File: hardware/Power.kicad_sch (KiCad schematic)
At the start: 19 parts, among them J10 DC, Q1 Q_NMOS, U10 ADP7142AUJZ-3.3, U11 ADP7142AUJZ-2.5, U12 LM74700, U13 ADP7142AUJZ-5.0

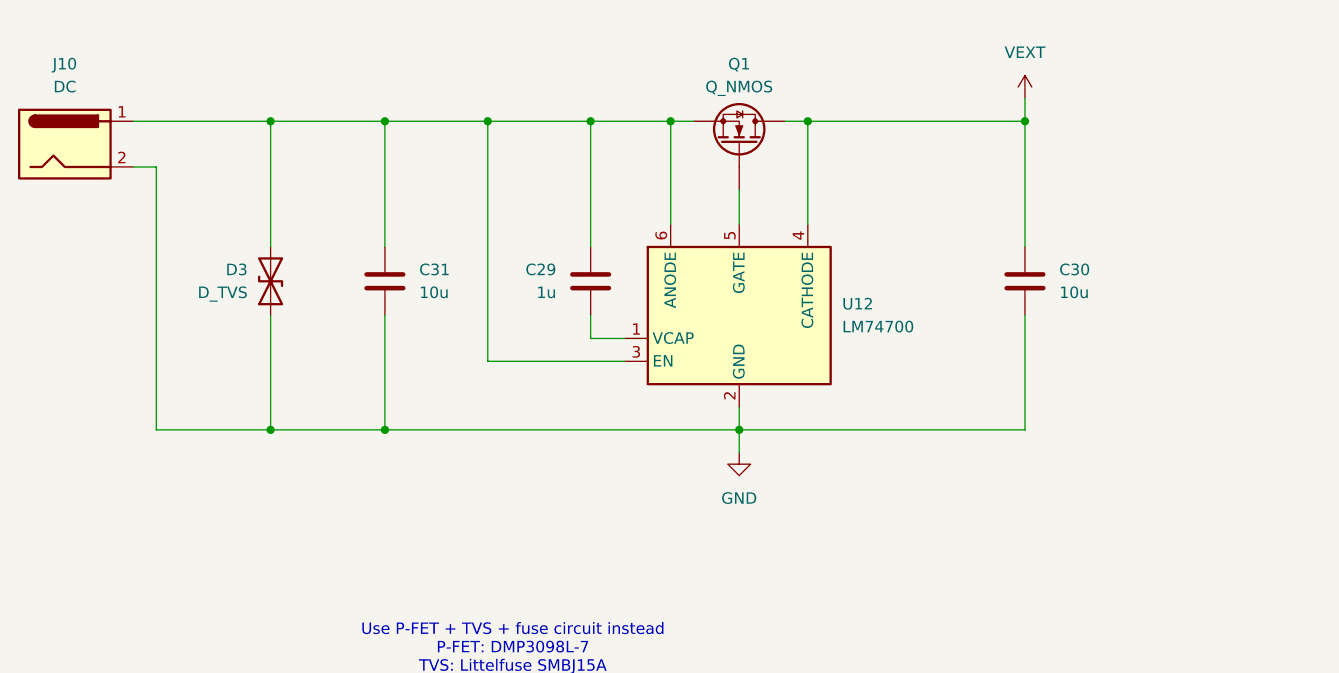
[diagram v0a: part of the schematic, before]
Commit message: updated Power input on schematic
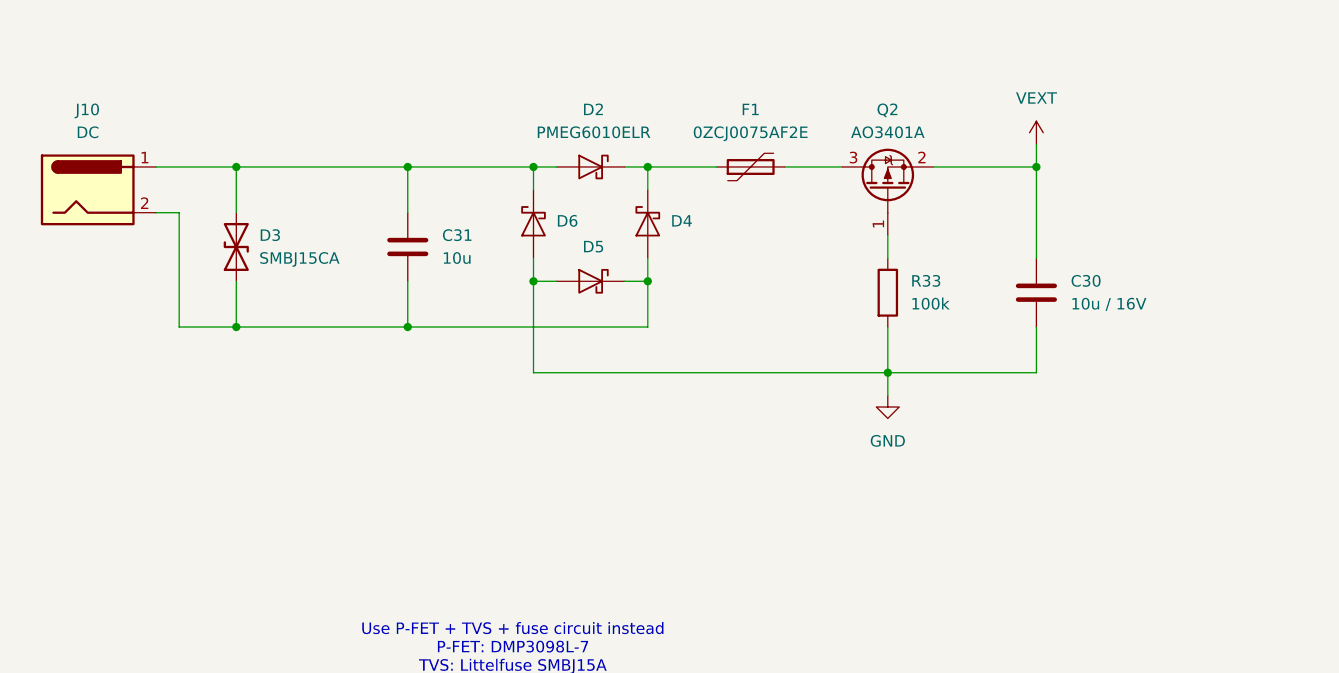
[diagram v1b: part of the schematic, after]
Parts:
- removed C29: 1u, Capacitor_SMD:C_0603_1608Metric, symbol Device:C
- removed Q1: Q_NMOS, symbol Device:Q_NMOS
- removed U12: LM74700, Package_TO_SOT_SMD:SOT-23-6, symbol Power_Management:LM74700
- added D2, D4, D5, D6: PMEG6010ELR, Diode_SMD:Nexperia_CFP3_SOD-123W, symbol Diode:PMEG6010ELR
- added F1: 0ZCJ0075AF2E, symbol Device:Polyfuse
- added Q2: AO3401A, Package_TO_SOT_SMD:SOT-23, symbol Transistor_FET:AO3401A
- added R33: 100k, symbol Device:R
- C30: value 10u -> 10u / 16V
- D3: value D_TVS -> SMBJ15CA
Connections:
- net GND: now also D5.2 (A), D6.2 (A), R33.2; no longer C31.2, D3.1 (A1), J10.2
- net VEXT: now also Q2.2 (S)
- net at C31.1, D3.2 (A2), J10.1: now also D2.2 (A), D6.1 (K)
- new net: D2.1 (K), D4.1 (K), F1.1
- new net: C31.2, D3.1 (A1), D4.2 (A), D5.1 (K), J10.2
- new net: Q2.1 (G), R33.1
- new net: F1.2, Q2.3 (D)
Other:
- moved on the sheet: C31, D3, J10

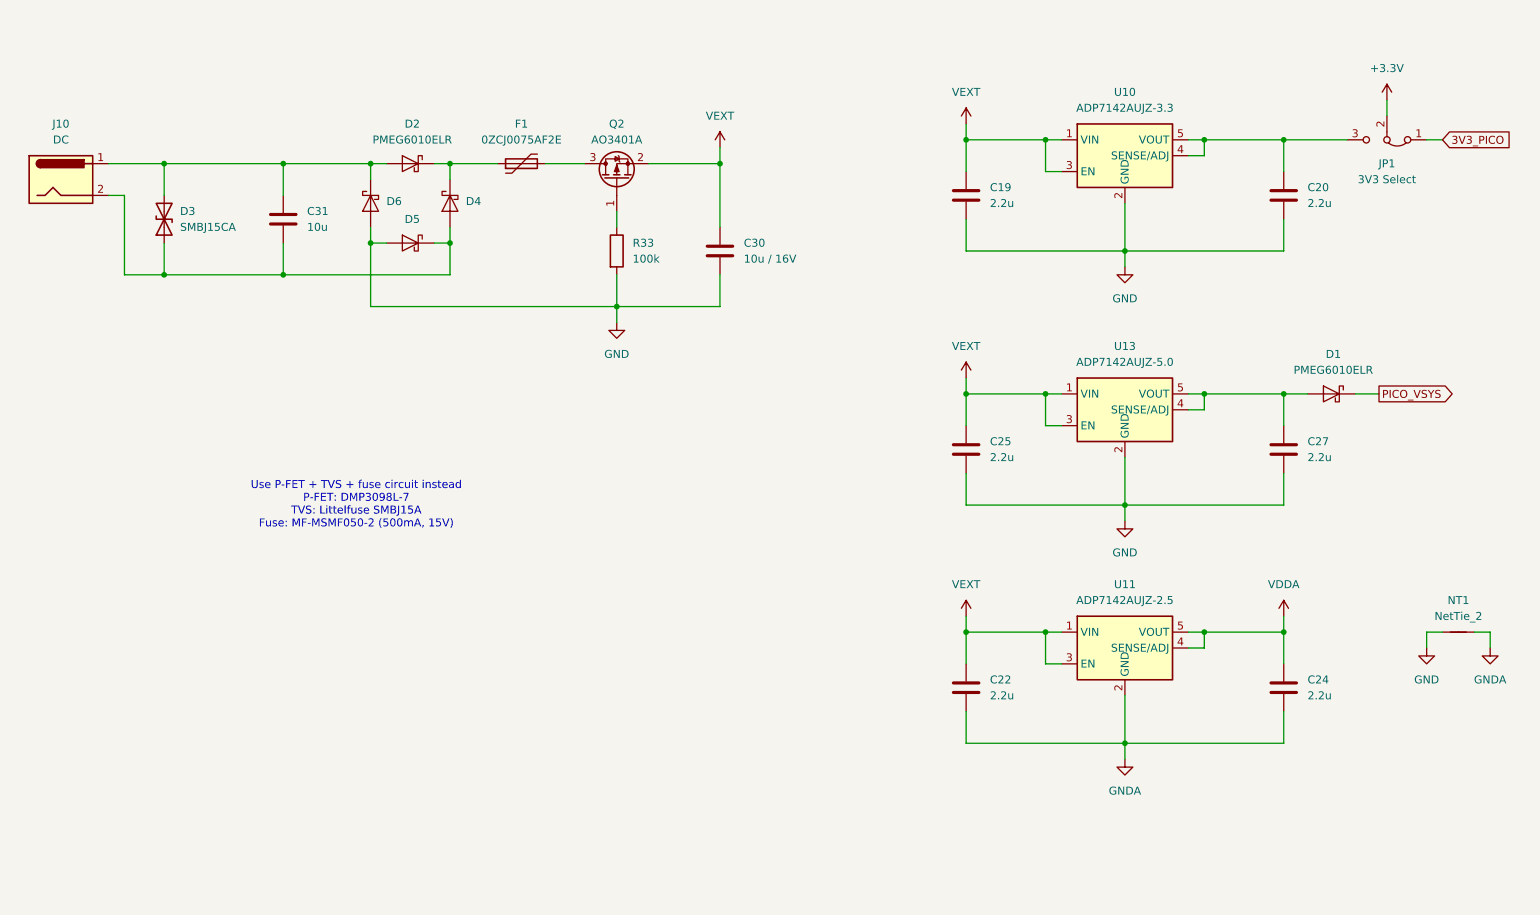
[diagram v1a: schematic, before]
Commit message: reworked power protection circuit and fixed ERC errors
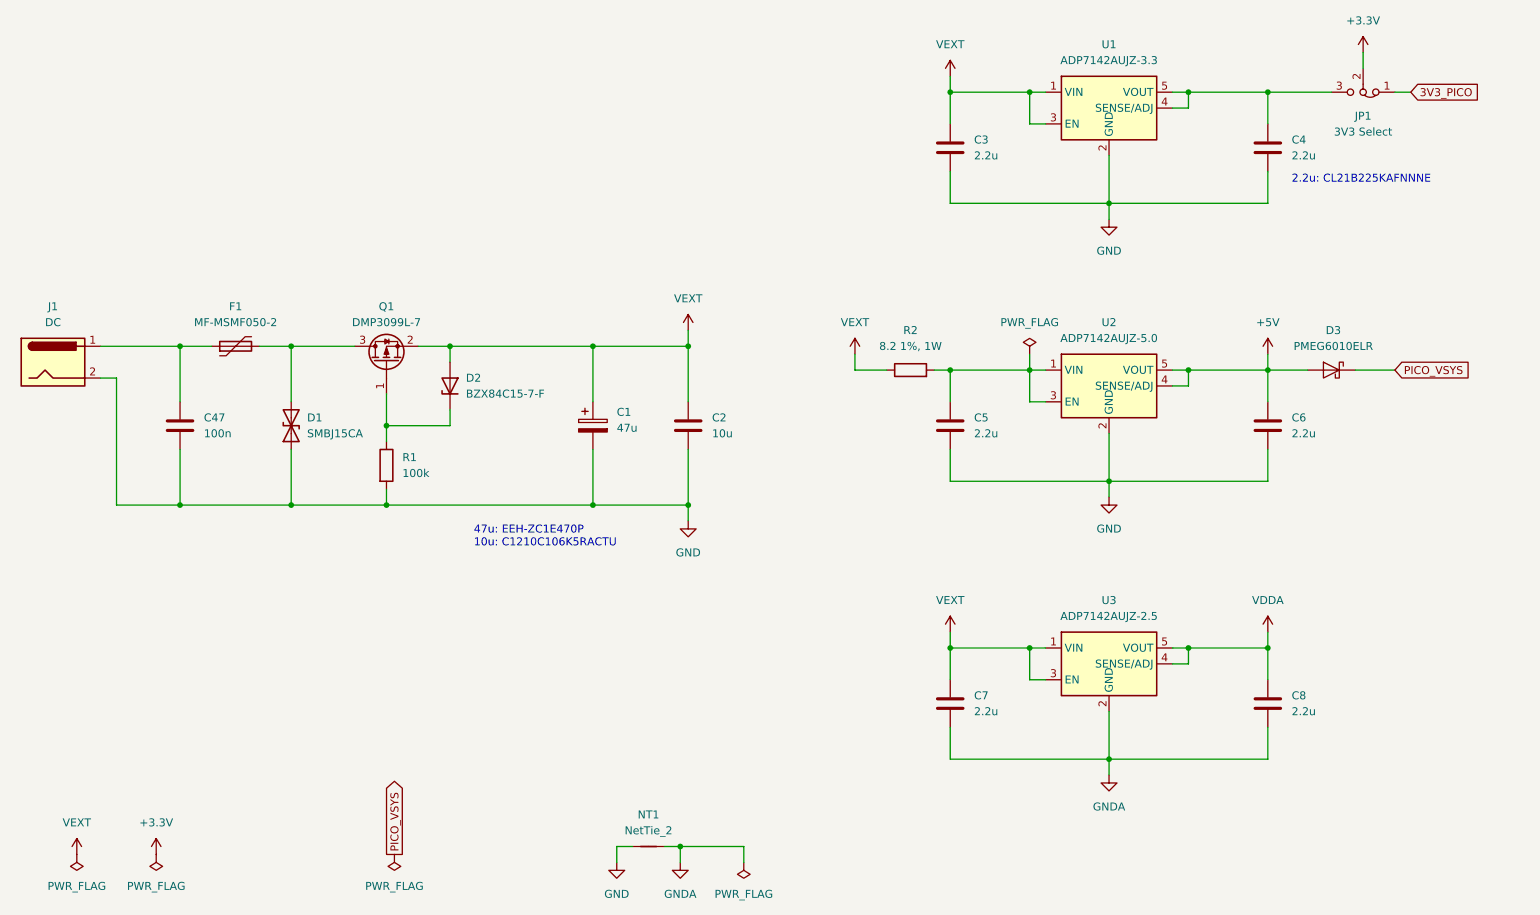
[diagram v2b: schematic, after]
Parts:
- removed C30: 10u / 16V, Capacitor_SMD:C_0603_1608Metric, symbol Device:C
- removed C31: 10u, Capacitor_SMD:C_0603_1608Metric, symbol Device:C
- removed D2, D4, D5, D6: PMEG6010ELR, Diode_SMD:Nexperia_CFP3_SOD-123W, symbol Diode:PMEG6010ELR
- removed D3: SMBJ15CA, symbol Device:D_TVS
- removed Q2: AO3401A, Package_TO_SOT_SMD:SOT-23, symbol Transistor_FET:AO3401A
- removed R33: 100k, symbol Device:R
- added C1: 47u, Capacitor_SMD:CP_Elec_6.3x5.8, symbol Device:C_Polarized
- added C2: 10u, Capacitor_SMD:C_1210_3225Metric, symbol Device:C
- added C47: 100n, Capacitor_SMD:C_0603_1608Metric, symbol Device:C
- added D1: SMBJ15CA, Diode_SMD:D_SMB, symbol Device:D_TVS
- added D2: BZX84C15-7-F, Package_TO_SOT_SMD:SOT-23, symbol Diode:BZX84Cxx
- added Q1: DMP3099L-7, Package_TO_SOT_SMD:SOT-23, symbol Transistor_FET:DMP3099L
- added R1: 100k, Resistor_SMD:R_0603_1608Metric, symbol Device:R
- added R2: 8.2 1%, 1W, Resistor_SMD:R_0603_1608Metric, symbol Device:R
- C3: renamed from C19; footprint Capacitor_SMD:C_0603_1608Metric -> Capacitor_SMD:C_0805_2012Metric
- C4: renamed from C20; footprint Capacitor_SMD:C_0603_1608Metric -> Capacitor_SMD:C_0805_2012Metric
- C5: renamed from C25; footprint Capacitor_SMD:C_0603_1608Metric -> Capacitor_SMD:C_0805_2012Metric
- C6: renamed from C27; footprint Capacitor_SMD:C_0603_1608Metric -> Capacitor_SMD:C_0805_2012Metric
- C7: renamed from C22; footprint Capacitor_SMD:C_0603_1608Metric -> Capacitor_SMD:C_0805_2012Metric
- C8: renamed from C24; footprint Capacitor_SMD:C_0603_1608Metric -> Capacitor_SMD:C_0805_2012Metric
- F1: value 0ZCJ0075AF2E -> MF-MSMF050-2; footprint (none) -> Fuse:Fuse_1812_4532Metric
- JP1: footprint (none) -> Connector_PinHeader_2.54mm:PinHeader_1x03_P2.54mm_Vertical
- NT1: footprint (none) -> NetTie:NetTie-2_SMD_Pad2.0mm
- renumbered D1 to D3, J10 to J1, U10 to U1, U13 to U2, U11 to U3
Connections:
- net GND: now also J1.2, C1.2, C2.2, C47.2, D1.1 (A1), R1.2
- net VEXT: now also C1.1, C2.1, D2.1 (A), Q1.2 (S), R2.1; no longer C5.1, U2.1 (VIN), U2.3 (EN)
- net at F1.1: now also J1.1, C47.1
- net +5V: now reaches C6.1, D3.2 (A), U2.4 (SENSE/ADJ), U2.5 (VOUT)
- net at F1.2: now also D1.2 (A2), Q1.3 (D)
- new net: D2.3 (K), Q1.1 (G), R1.1
- new net: C5.1, R2.2, U2.1 (VIN), U2.3 (EN)
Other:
- note added: "2.2u: CL21B225KAFNNNE"
- note added: "47u: EEH-ZC1E470P 10u: C1210C106K5RACTU"
- note removed: "Use P-FET + TVS + fuse circuit instead P-FET: DMP3098L-7 TVS: Littelfuse SMBJ15A Fuse: MF-MSMF050-2 (500mA, 15V)"
- moved on the sheet: C3, C4, C5, C6, C7, C8, D3, J1, JP1, NT1, U1, U2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

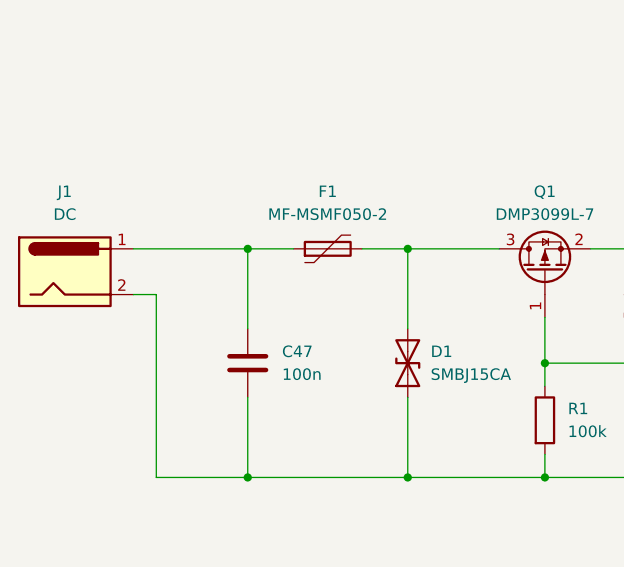
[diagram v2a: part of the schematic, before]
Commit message: added basic PCB ordering
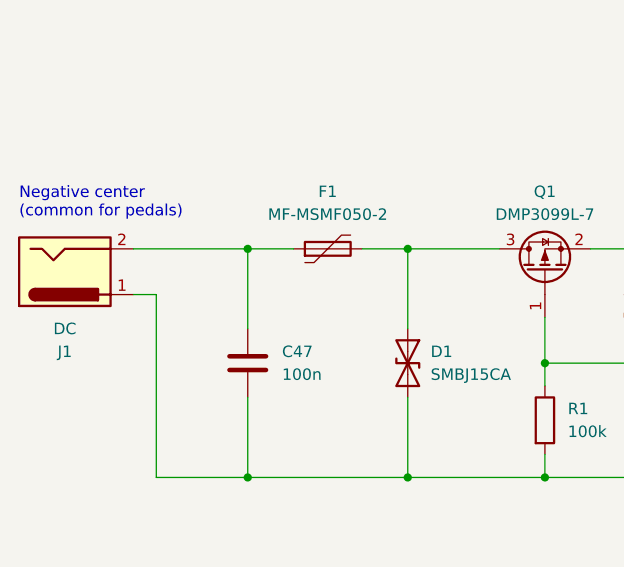
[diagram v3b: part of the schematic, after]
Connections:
- net GND: now also D1.2 (A2), J1.1; no longer D1.1 (A1), J1.2
- net at F1.2, Q1.3 (D): now also D1.1 (A1); no longer D1.2 (A2)
- net at C47.1, F1.1: now also J1.2; no longer J1.1
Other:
- note added: "Negative center (common for pedals)"
- moved on the sheet: D1
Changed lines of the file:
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@@
 		)
 	)
+	(text "Negative center\n(common for pedals)"
+		(exclude_from_sim no)
+		(at 29.21 71.12 0)
+		(effects
+			(font
+				(size 1.27 1.27)
+			)
+			(justify left)
+		)
+	)
 	(text "47u: EEH-ZC1E470P\n10u: C1210C106K5RACTU"
 		(exclude_from_sim no)
@@
 	(symbol
 		(lib_id "Device:D_TVS")
-		(at 72.39 88.9 90)
+		(at 72.39 88.9 270)
 		(unit 1)
 		(body_style 1)
@@
 					(size 1.27 1.27)
 				)
-				(justify right)
+				(justify left)
 			)
 		)
@@
 					(size 1.27 1.27)
 				)
-				(justify right)
+				(justify left)
 			)
 		)
@@
 		(lib_id "Connector:Barrel_Jack")
 		(at 34.29 78.74 0)
+		(mirror x)
 		(unit 1)
 		(body_style 1)
@@
 		(in_pos_files yes)
 		(dnp no)
-		(fields_autoplaced yes)
 		(property "Reference" "J1"
-			(at 34.29 69.85 0)
+			(at 34.29 87.63 0)
 			(show_name no)
 			(do_not_autoplace no)
@@
 		)
 		(property "Value" "DC"
-			(at 34.29 72.39 0)
+			(at 34.29 85.09 0)
 			(show_name no)
 			(do_not_autoplace no)
@@
 		)
 		(property "Footprint" ""
-			(at 35.56 79.756 0)
+			(at 35.56 77.724 0)
 			(hide yes)
 			(show_name no)
@@
 		)
 		(property "Datasheet" ""
-			(at 35.56 79.756 0)
+			(at 35.56 77.724 0)
 			(hide yes)
 			(show_name no)

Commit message: added all footprints, updated to 0805, added layout for Jacks
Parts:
- C47: footprint Capacitor_SMD:C_0603_1608Metric -> Capacitor_SMD:C_0805_2012Metric
- J1: footprint (none) -> Connector_BarrelJack:BarrelJack_CUI_PJ-102AH_Horizontal; symbol Connector:Barrel_Jack -> Connector:Barrel_Jack_Switch
- R1, R2: footprint Resistor_SMD:R_0603_1608Metric -> Resistor_SMD:R_0805_2012Metric
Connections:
- no-connect marks 0 -> 1
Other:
- note added: "center negative (common for pedals)"
- note removed: "Negative center (common for pedals)"
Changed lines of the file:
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@@
 		)
 	)
-	(text "Negative center\n(common for pedals)"
+	(text "center negative\n(common for pedals)"
 		(exclude_from_sim no)
 		(at 29.21 71.12 0)
@@
 		(color 0 0 0 0)
 	)
+	(no_connect
+		(at 41.91 78.74)
+	)
 	(wire
 		(pts
@@
 			)
 		)
-		(property "Footprint" "Resistor_SMD:R_0603_1608Metric"
+		(property "Footprint" "Resistor_SMD:R_0805_2012Metric"
 			(at 85.852 95.25 90)
 			(hide yes)
@@
 			)
 		)
-		(property "Footprint" "Resistor_SMD:R_0603_1608Metric"
+		(property "Footprint" "Resistor_SMD:R_0805_2012Metric"
 			(at 171.45 81.788 90)
 			(hide yes)
@@
 			)
 		)
-		(property "Footprint" "Capacitor_SMD:C_0603_1608Metric"
+		(property "Footprint" "Capacitor_SMD:C_0805_2012Metric"
 			(at 55.5752 92.71 0)
 			(hide yes)
@@
 	)
 	(symbol
-		(lib_id "Connector:Barrel_Jack")
+		(lib_id "Connector:Barrel_Jack_Switch")
 		(at 34.29 78.74 0)
 		(mirror x)
@@
 			)
 		)
-		(property "Footprint" ""
+		(property "Footprint" "Connector_BarrelJack:BarrelJack_CUI_PJ-102AH_Horizontal"
 			(at 35.56 77.724 0)
 			(hide yes)
@@
 			)
 		)
-		(property "Description" "DC Barrel Jack"
+		(property "Description" "DC Barrel Jack with an internal switch"
 			(at 34.29 78.74 0)
 			(hide yes)
@@
 		(pin "2"
 		)
+		(pin "3"
+		)
 		(instances

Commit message: schematic updates
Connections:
- net VDDA renamed +2.5V
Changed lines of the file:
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@@
+	)
+	(symbol
+		(lib_id "PowerSymbols:+2.5V")
+		(at 228.6 121.92 0)
+		(unit 1)
+		(body_style 1)
+		(exclude_from_sim no)
+		(in_bom yes)
+		(on_board yes)
+		(in_pos_files yes)
+		(dnp no)
+		(fields_autoplaced yes)
+		(property "Reference" "#PWR064"
+			(at 228.6 125.73 0)
+			(hide yes)
+			(show_name no)
+			(do_not_autoplace no)
+			(effects
+				(font
+					(size 1.27 1.27)
+				)
+			)
+		)
+		(property "Value" "+2.5V"
+			(at 228.6 116.84 0)
+			(show_name no)
+			(do_not_autoplace no)
+			(effects
+				(font
+					(size 1.27 1.27)
+				)
+			)
+		)
+		(property "Footprint" ""
+			(at 228.6 121.92 0)
+			(hide yes)
+			(show_name no)
+			(do_not_autoplace no)
+			(effects
+				(font
+					(size 1.27 1.27)
+				)
+			)
+		)
+		(property "Datasheet" ""
+			(at 228.6 121.92 0)
+			(hide yes)
+			(show_name no)
+			(do_not_autoplace no)
+			(effects
+				(font
+					(size 1.27 1.27)
+				)
+			)
+		)
+		(property "Description" "Power symbol creates a global label with name \"+3.3V\""
+			(at 228.6 121.92 0)
+			(hide yes)
+			(show_name no)
+			(do_not_autoplace no)
+			(effects
+				(font
+					(size 1.27 1.27)
+				)
+			)
+		)
+		(pin "1"
+		)
+		(instances
+			(project "ExpressionController"
+				(path "/acb9d00b-1122-4203-9813-1d558ab77d86/70b13573-959f-46df-b1fb-aa39c60a59ac"
+					(reference "#PWR064")
+					(unit 1)
+				)
+			)
+		)
 	)
 	(symbol
@@
 					(unit 1)
 				)
-			)
-		)
-	)
-	(symbol
-		(lib_id "power:VDDA")
-		(at 228.6 121.92 0)
-		(unit 1)
-		(body_style 1)
-		(exclude_from_sim no)
-		(in_bom yes)
-		(on_board yes)
-		(in_pos_files yes)
-		(dnp no)
-		(fields_autoplaced yes)
-		(property "Reference" "#PWR064"
-			(at 228.6 125.73 0)
-			(hide yes)
-			(show_name no)
-			(do_not_autoplace no)
-			(effects
-				(font
-					(size 1.27 1.27)
-				)
-			)
-		)
-		(property "Value" "VDDA"
-			(at 228.6 116.84 0)
-			(show_name no)
-			(do_not_autoplace no)
-			(effects
-				(font
-					(size 1.27 1.27)
-				)
-			)
-		)
-		(property "Footprint" ""
-			(at 228.6 121.92 0)
-			(hide yes)
-			(show_name no)
-			(do_not_autoplace no)
-			(effects
-				(font
-					(size 1.27 1.27)
-				)
-			)
-		)
-		(property "Datasheet" ""
-			(at 228.6 121.92 0)
-			(hide yes)
-			(show_name no)
-			(do_not_autoplace no)
-			(effects
-				(font
-					(size 1.27 1.27)
-				)
-			)
-		)
-		(property "Description" "Power symbol creates a global label with name \"VDDA\""
-			(at 228.6 121.92 0)
-			(hide yes)
-			(show_name no)
-			(do_not_autoplace no)
-			(effects
-				(font
-					(size 1.27 1.27)
-				)
-			)
-		)
-		(pin "1"
-		)
-		(instances
-			(project "ExpressionController"
-				(path "/acb9d00b-1122-4203-9813-1d558ab77d86/70b13573-959f-46df-b1fb-aa39c60a59ac"
-					(reference "#PWR064")
-					(unit 1)
-				)

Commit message: replaced buffer ICs with analog switches, schematic bugfixes, started new routing
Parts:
- removed C7: 2.2u, Capacitor_SMD:C_0805_2012Metric, symbol Device:C
- removed JP1: 3V3 Select, Connector_PinHeader_2.54mm:PinHeader_1x03_P2.54mm_Vertical, symbol Jumper:Jumper_3_Bridged12
- removed NT1: NetTie_2, NetTie:NetTie-2_SMD_Pad2.0mm, symbol Device:NetTie_2
- removed R2: 8.2 1%, 1W, Resistor_SMD:R_0805_2012Metric, symbol Device:R
- C2: footprint Capacitor_SMD:C_1210_3225Metric -> Capacitor_SMD:C_0805_2012Metric
- C3, C5: value 2.2u -> 4.7u
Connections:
- net GNDA is gone; now on net GND: C8.2, U3.2 (GND)
- net VEXT: now also C5.1, D2.3 (K), U2.1 (VIN), U2.3 (EN); no longer D2.1 (A), U3.1 (VIN), U3.3 (EN)
- net at Q1.1 (G), R1.1: now also D2.1 (A); no longer D2.3 (K)
- net +3.3VA: now reaches C4.1, U1.4 (SENSE/ADJ), U1.5 (VOUT)
- net +3.3VA: now also U3.1 (VIN), U3.3 (EN)
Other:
- moved on the sheet: C3, C4, C5, C6, D2, D3, U1, U2

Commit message: added mouser part numbers
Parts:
- C1: Mouser No (none) -> 667-EEH-ZC1E470P; Part Source (none) -> Mouser
- C2: Notes (none) -> im Uni-Sortiment?; Part Source (none) -> Uni
- C3, C4, C47, C5, C6, C8, R1: Part Source (none) -> Uni
- D1: Mouser No (none) -> 947-SMBJ15CA; Part Source (none) -> Mouser
- D2: Mouser No (none) -> 621-BZX84C15-F; Part Source (none) -> Mouser
- D3: Mouser No (none) -> 771-PMEG6010ELRX; Part Source (none) -> Mouser
- F1: Mouser No (none) -> 652-MF-MSMF050-2; Part Source (none) -> Mouser
- J1: value DC -> BarrelJack; Mouser No (none) -> 490-PJ-102AH; Part Source (none) -> Mouser
- Q1: Mouser No (none) -> 621-DMP3099L-7; Part Source (none) -> Mouser
- U1: Mouser No (none) -> 584-ADP7142AUJZ3.3R7; Part Source (none) -> Mouser
- U2: Mouser No (none) -> 584-ADP7142WAUJZ-50R; Part Source (none) -> Mouser
- U3: Mouser No (none) -> 584-ADP7142AUJZ2.5R7; Part Source (none) -> Mouser

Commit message: added testpoints
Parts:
- added TP12, TP13, TP14, TP15: TestPoint, TestPoint:TestPoint_THTPad_D1.5mm_Drill0.7mm, symbol Connector:TestPoint
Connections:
- net +2.5V: now also TP14.1
- net +3.3VA: now also TP13.1
- net +5V: now also TP12.1
- net VEXT: now also TP15.1
